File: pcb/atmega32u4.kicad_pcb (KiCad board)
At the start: 2 copper layers, 21 parts, among them CON1 ISP, P1 CONN_01X14, P2 CONN_01X14, P3 USB_OTG, SW1 SW_PUSH, U1 ATmega32U4-AU, Y1 16MHz

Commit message: I think I'm done?
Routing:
- net GND: track 48.7 -> 153.8 mm, vias 4 -> 8
- net +5V: track 26.4 -> 111.6 mm, vias 1 -> 3
- net VCC: track 35.0 -> 98.7 mm, vias 0 -> 4
- net /PE6: track 2.80 -> 59.8 mm, vias 1 -> 3
- net /XTAL1: track 0.00 -> 40.2 mm, vias 0 -> 2
- net /PB7: track 1.42 -> 36.7 mm
- net /XTAL2: track 0.00 -> 32.5 mm, vias 0 -> 1
- net /ISP_RESET: track 55.9 -> 70.5 mm, vias 1 -> 3
- net Net-(D2-Pad2): track 0.00 -> 2.99 mm
- net Net-(D1-Pad2): track 0.00 -> 2.99 mm

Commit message: add edge cuts
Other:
- board outline added: 24.1 x 67.3 mm
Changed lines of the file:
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@@
     (links 80)
     (no_connects 0)
-    (area 123.284267 79.9976 178.94281 149.496209)
+    (area 126.289999 83.109999 150.570001 150.570001)
     (thickness 1.6)
-    (drawings 28)
+    (drawings 34)
     (tracks 324)
     (zones 0)
@@
       (effects (font (size 1 1) (thickness 0.15)))
     )
-    (fp_text value 1K (at -1 -2.1 270) (layer F.SilkS)
+    (fp_text value 1K (at 1.3 -2.1 270) (layer F.SilkS)
       (effects (font (size 0.75 0.75) (thickness 0.1)))
     )
@@
       (effects (font (size 1 1) (thickness 0.15)))
     )
-    (fp_text value 1K (at -1 2.1 270) (layer F.SilkS)
+    (fp_text value 1K (at 1.3 2.1 270) (layer F.SilkS)
       (effects (font (size 0.75 0.75) (thickness 0.1)))
     )
@@
     )
   )
+  (gr_line (start 126.365 150.495) (end 126.365 149.86) (angle 90) (layer Edge.Cuts) (width 0.15))
+  (gr_line (start 150.495 150.495) (end 126.365 150.495) (angle 90) (layer Edge.Cuts) (width 0.15))
+  (gr_line (start 150.495 149.86) (end 150.495 150.495) (angle 90) (layer Edge.Cuts) (width 0.15))
+  (gr_line (start 126.365 149.86) (end 126.365 83.185) (angle 90) (layer Edge.Cuts) (width 0.15))
+  (gr_line (start 150.495 83.185) (end 150.495 149.86) (angle 90) (layer Edge.Cuts) (width 0.15))
+  (gr_line (start 126.365 83.185) (end 150.495 83.185) (angle 90) (layer Edge.Cuts) (width 0.15))
   (gr_text PF7 (at 177.419 126.619) (layer F.SilkS)
     (effects (font (size 1 1) (thickness 0.15)))

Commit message: Finished dat board
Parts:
- R4, R5: value 1K -> 1kΩ
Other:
- board text added: "5V"
- board text added: "B0"
- board text added: "B1"
- board text added: "B2"
- board text added: "B3"
- board text added: "B4"
- board text added: "B5"
- board text added: "B6"
- board text added: "B7"
- board text added: "C6"
- board text added: "C7"
- board text added: "D0"
- board text added: "D1"
- board text added: "D2"
- board text added: "D3"
- board text added: "D4"
- board text added: "D5"
- board text added: "D6"
- board text added: "D7"
- board text added: "E6"
- board text added: "F0"
- board text added: "F1"
- board text added: "F4"
- board text added: "F5"
- board text added: "F6"
- board text added: "F7"
- board text removed: "PB0"
- board text removed: "PB1"
- board text removed: "PB2"
- board text removed: "PB3"
- board text removed: "PB4"
- board text removed: "PB5"
- board text removed: "PB6"
- board text removed: "PB7"
- board text removed: "PC6"
- board text removed: "PC7"
- board text removed: "PD0"
- board text removed: "PD1"
- board text removed: "PD2"
- board text removed: "PD3"
- board text removed: "PD4"
- board text removed: "PD5"
- board text removed: "PD6"
- board text removed: "PD7"
- board text removed: "PF0"
- board text removed: "PF4"
- board text removed: "PF5"
- board text removed: "PF6"
- board text removed: "PF7"
- board text removed: "VCC"

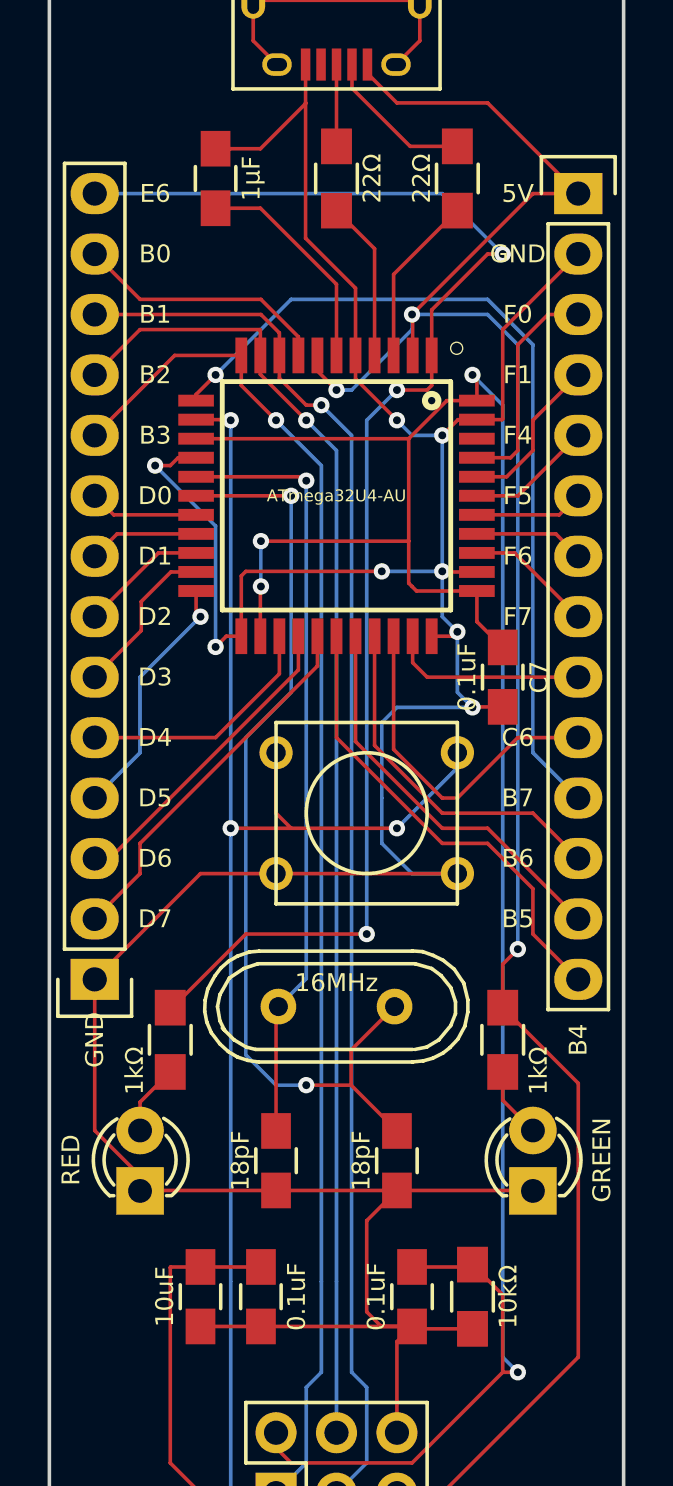
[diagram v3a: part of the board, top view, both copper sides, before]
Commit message: Relabel components
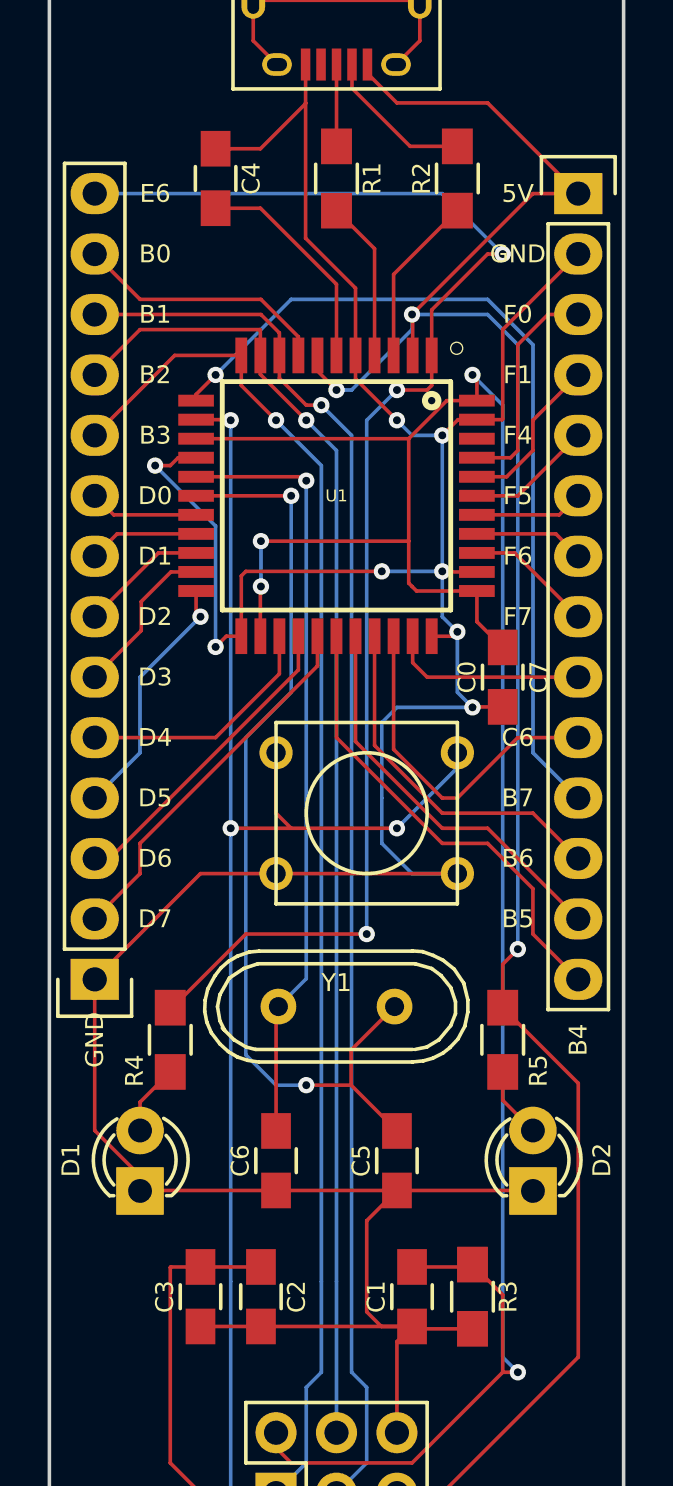
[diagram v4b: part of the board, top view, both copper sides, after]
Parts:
- C0: value 0.1uF -> C0
- C1: value 0.1uF -> C1
- C2: value 0.1uF -> C2
- C3: value 10uF -> C3
- C4: value 1µF -> C4
- C5: value 18pF -> C5
- C6: value 18pF -> C6
- D1: value RED -> D1
- D2: value GREEN -> D2
- R1: value 22Ω -> R1
- R2: value 22Ω -> R2
- R3: value 10kΩ -> R3
- R4: value 1kΩ -> R4
- R5: value 1kΩ -> R5
- U1: value ATmega32U4-AU -> U1
- Y1: value 16MHz -> Y1
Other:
- net class Default: clearance 0.1524 -> 0.2; trace_width 0.1524 -> 0.25; via_dia 0.6858 -> 0.6; via_drill 0.3302 -> 0.4
- rule trace_clearance: 0.1524 -> 0.2
- rule trace_min: 0.1524 -> 0.13
- rule via_min_drill: 0.3302 -> 0.305
- rule via_min_size: 0.6858 -> 0.465
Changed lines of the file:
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@@
     (links 80)
     (no_connects 0)
-    (area 126.289999 83.109999 150.570001 150.570001)
+    (area 123.284267 79.9976 153.575734 150.570001)
     (thickness 1.6)
     (drawings 34)
@@
   )
   (setup
-    (last_trace_width 0.1524)
-    (trace_clearance 0.1524)
+    (last_trace_width 0.25)
+    (trace_clearance 0.2)
     (zone_clearance 0.508)
     (zone_45_only no)
-    (trace_min 0.1524)
+    (trace_min 0.13)
     (segment_width 0.2)
     (edge_width 0.15)
-    (via_size 0.6858)
-    (via_drill 0.3302)
-    (via_min_size 0.6858)
-    (via_min_drill 0.3302)
-    (uvia_size 0.762)
-    (uvia_drill 0.508)
-    (uvias_allowed no)
-    (uvia_min_size 0)
-    (uvia_min_drill 0)
+    (via_size 0.6)
+    (via_drill 0.4)
+    (via_min_size 0.465)
+    (via_min_drill 0.305)
+    (uvia_size 0.51)
+    (uvia_drill 0.13)
+    (uvias_allowed yes)
+    (uvia_min_size 0.18)
+    (uvia_min_drill 0.1)
     (pcb_text_width 0.3)
     (pcb_text_size 1.5 1.5)
@@
   (net 41 "Net-(D2-Pad2)")
   (net_class Default "This is the default net class."
-    (clearance 0.1524)
-    (trace_width 0.1524)
-    (via_dia 0.6858)
-    (via_drill 0.3302)
-    (uvia_dia 0.762)
-    (uvia_drill 0.508)
+    (clearance 0.2)
+    (trace_width 0.25)
+    (via_dia 0.6)
+    (via_drill 0.4)
+    (uvia_dia 0.51)
+    (uvia_drill 0.13)
     (add_net +5V)
     (add_net /ISP_MISO/PB3)
@@
       (effects (font (size 1 1) (thickness 0.15)))
     )
-    (fp_text value 0.1uF (at 0 1.5 270) (layer F.SilkS)
+    (fp_text value C1 (at 0 1.5 270) (layer F.SilkS)
       (effects (font (size 0.75 0.75) (thickness 0.1)))
     )
@@
       (effects (font (size 1 1) (thickness 0.15)))
     )
-    (fp_text value 0.1uF (at 0 -1.5 270) (layer F.SilkS)
+    (fp_text value C2 (at 0 -1.5 270) (layer F.SilkS)
       (effects (font (size 0.75 0.75) (thickness 0.1)))
     )
@@
       (effects (font (size 1 1) (thickness 0.15)))
     )
-    (fp_text value 10uF (at 0 1.5 270) (layer F.SilkS)
+    (fp_text value C3 (at 0 1.5 270) (layer F.SilkS)
       (effects (font (size 0.75 0.75) (thickness 0.1)))
     )
@@
       (effects (font (size 1 1) (thickness 0.15)))
     )
-    (fp_text value 1µF (at 0 1.5 90) (layer F.SilkS)
+    (fp_text value C4 (at 0 1.5 90) (layer F.SilkS)
       (effects (font (size 0.75 0.75) (thickness 0.1)))
     )
@@
       (effects (font (size 1 1) (thickness 0.15)))
     )
-    (fp_text value 18pF (at 0 1.5 270) (layer F.SilkS)
+    (fp_text value C5 (at 0 1.5 270) (layer F.SilkS)
       (effects (font (size 0.75 0.75) (thickness 0.1)))
     )
@@
       (effects (font (size 1 1) (thickness 0.15)))
     )
-    (fp_text value 18pF (at 0 1.5 270) (layer F.SilkS)
+    (fp_text value C6 (at 0 1.5 270) (layer F.SilkS)
       (effects (font (size 0.75 0.75) (thickness 0.1)))
     )
@@
       (effects (font (size 1 1) (thickness 0.15)))
     )
-    (fp_text value 22Ω (at 0 1.5 90) (layer F.SilkS)
+    (fp_text value R1 (at 0 1.5 90) (layer F.SilkS)
       (effects (font (size 0.75 0.75) (thickness 0.1)))
     )
@@
       (effects (font (size 1 1) (thickness 0.15)))
     )
-    (fp_text value 22Ω (at 0 -1.5 90) (layer F.SilkS)
+    (fp_text value R2 (at 0 -1.5 90) (layer F.SilkS)
       (effects (font (size 0.75 0.75) (thickness 0.1)))
     )
@@
       (effects (font (size 1 1) (thickness 0.15)))
     )
-    (fp_text value 10kΩ (at 0 -1.5 270) (layer F.SilkS)
+    (fp_text value R3 (at 0 -1.5 270) (layer F.SilkS)
       (effects (font (size 0.75 0.75) (thickness 0.1)))
     )
@@
       (effects (font (size 1.4 1.4) (thickness 0.05)))
     )
-    (fp_text value ATmega32U4-AU (at 0 0 360) (layer F.SilkS)
+    (fp_text value U1 (at 0 0 360) (layer F.SilkS)
       (effects (font (size 0.5 0.5) (thickness 0.1)))
     )
@@
       (effects (font (size 1 1) (thickness 0.15)))
     )
-    (fp_text value 16MHz (at 0 1 180) (layer F.SilkS)
+    (fp_text value Y1 (at 0 1 180) (layer F.SilkS)
       (effects (font (size 0.75 0.75) (thickness 0.1)))
     )
@@
       (effects (font (size 1 1) (thickness 0.15)))
     )
-    (fp_text value 0.1uF (at 0 1.5 270) (layer F.SilkS)
+    (fp_text value C0 (at 0 1.5 270) (layer F.SilkS)
       (effects (font (size 0.75 0.75) (thickness 0.1)))
     )
@@
       (effects (font (size 1 1) (thickness 0.15)))
     )
-    (fp_text value 1kΩ (at 1.3 1.5 270) (layer F.SilkS)
+    (fp_text value R4 (at 1.3 1.5 270) (layer F.SilkS)
       (effects (font (size 0.75 0.75) (thickness 0.1)))
     )
@@
       (effects (font (size 1 1) (thickness 0.15)))
     )
-    (fp_text value 1kΩ (at 1.3 -1.5 270) (layer F.SilkS)
+    (fp_text value R5 (at 1.3 -1.5 270) (layer F.SilkS)
       (effects (font (size 0.75 0.75) (thickness 0.1)))
     )
@@
       (effects (font (size 1 1) (thickness 0.15)))
     )
-    (fp_text value GREEN (at 1.3 2.9 90) (layer F.SilkS)
+    (fp_text value D2 (at 1.3 2.9 90) (layer F.SilkS)
       (effects (font (size 0.75 0.75) (thickness 0.1)))
     )
@@
       (effects (font (size 1 1) (thickness 0.15)))
     )
-    (fp_text value RED (at 1.3 -2.9 90) (layer F.SilkS)
-      (effects (font (size 0.75 0.75) (thickness 0.1)))
-    )
+    (fp_text value D1 (at 1.3 -2.9 90) (layer F.SilkS)
+      (effects (font (size 0.75 0.75) (thickness 0.1)))
+    )
